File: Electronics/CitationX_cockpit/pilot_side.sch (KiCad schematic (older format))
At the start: 18 parts

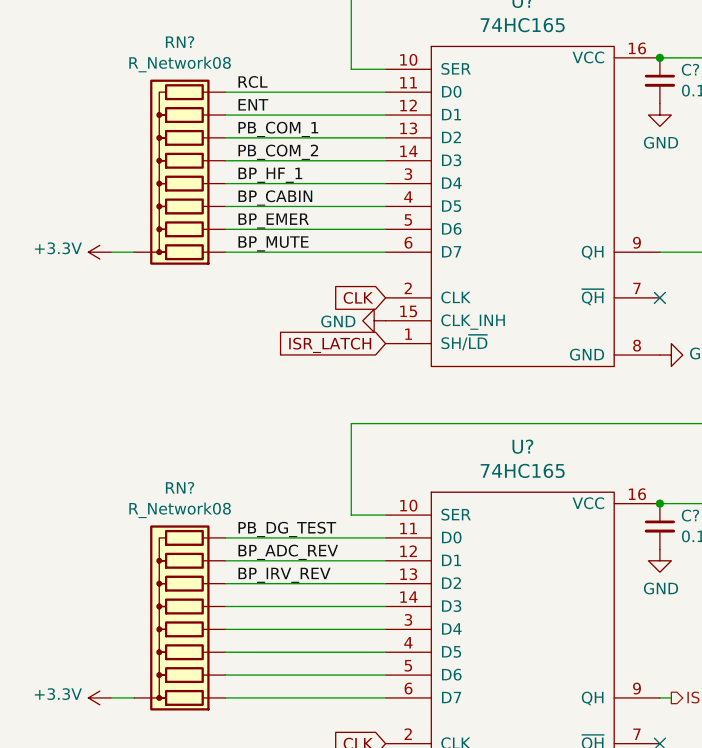
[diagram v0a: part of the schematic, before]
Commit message: Electronics - Working on copilot side and APU
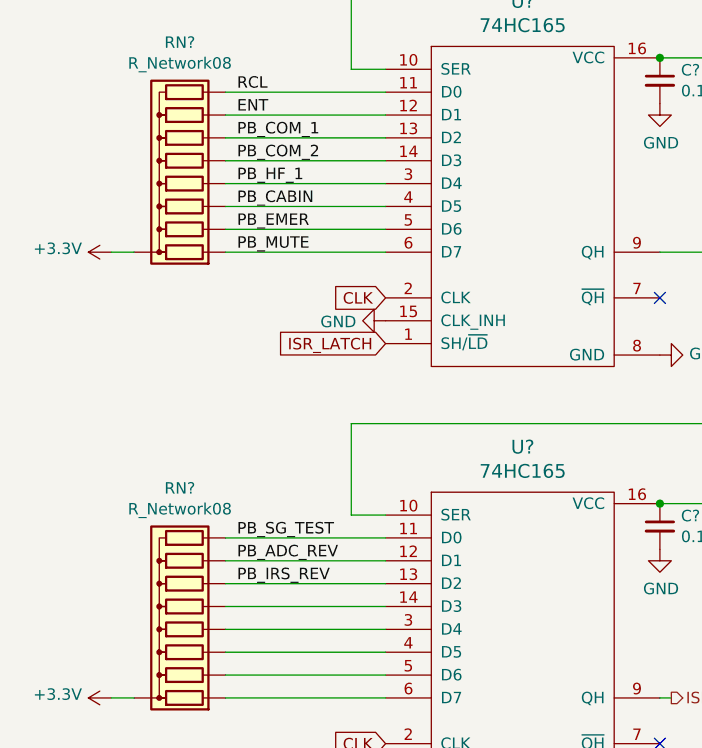
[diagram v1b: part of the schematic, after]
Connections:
- net BP_ADC_REV renamed PB_ADC_REV
- net BP_CABIN renamed PB_CABIN
- net BP_EMER renamed PB_EMER
- net BP_HF_1 renamed PB_HF_1
- net BP_IRV_REV renamed PB_IRS_REV
- net BP_MUTE renamed PB_MUTE
- net PB_DG_TEST renamed PB_SG_TEST
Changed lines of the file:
@@
 PB_COM_2
 Text Label 1600 5350 0    50   ~ 0
-BP_HF_1
+PB_HF_1
 Text Label 1600 5450 0    50   ~ 0
-BP_CABIN
+PB_CABIN
 Text Label 1600 5550 0    50   ~ 0
-BP_EMER
+PB_EMER
 Text Label 1600 5650 0    50   ~ 0
-BP_MUTE
+PB_MUTE
 Text Label 1600 6900 0    50   ~ 0
-PB_DG_TEST
+PB_SG_TEST
 Text Label 1600 7000 0    50   ~ 0
-BP_ADC_REV
+PB_ADC_REV
 Text Label 1600 7100 0    50   ~ 0
-BP_IRV_REV
+PB_IRS_REV
 $Comp
 L Device:C_Small C?

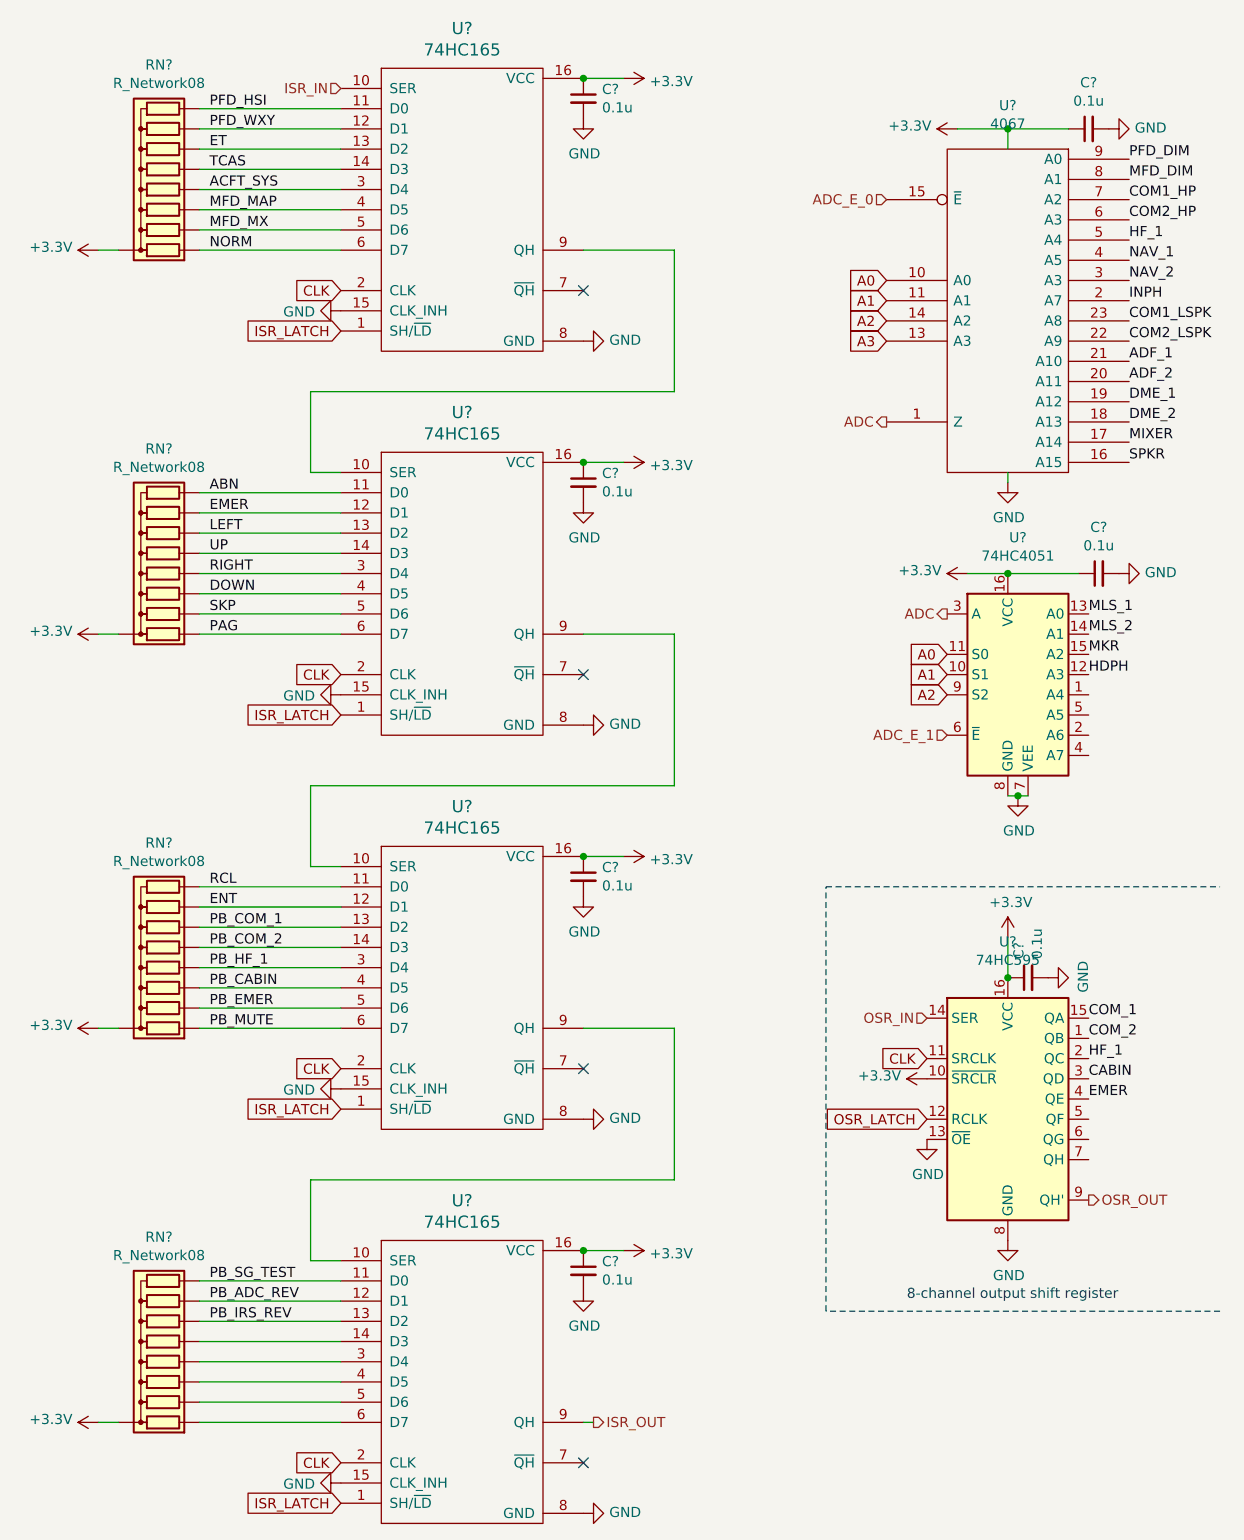
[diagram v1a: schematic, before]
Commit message: Electronics - Misc. works
Continued (and checked board). All connections are probably OK.
Fixed hierarchical pins in APUs (affects all schematics)
Numbered elements for testing schematics
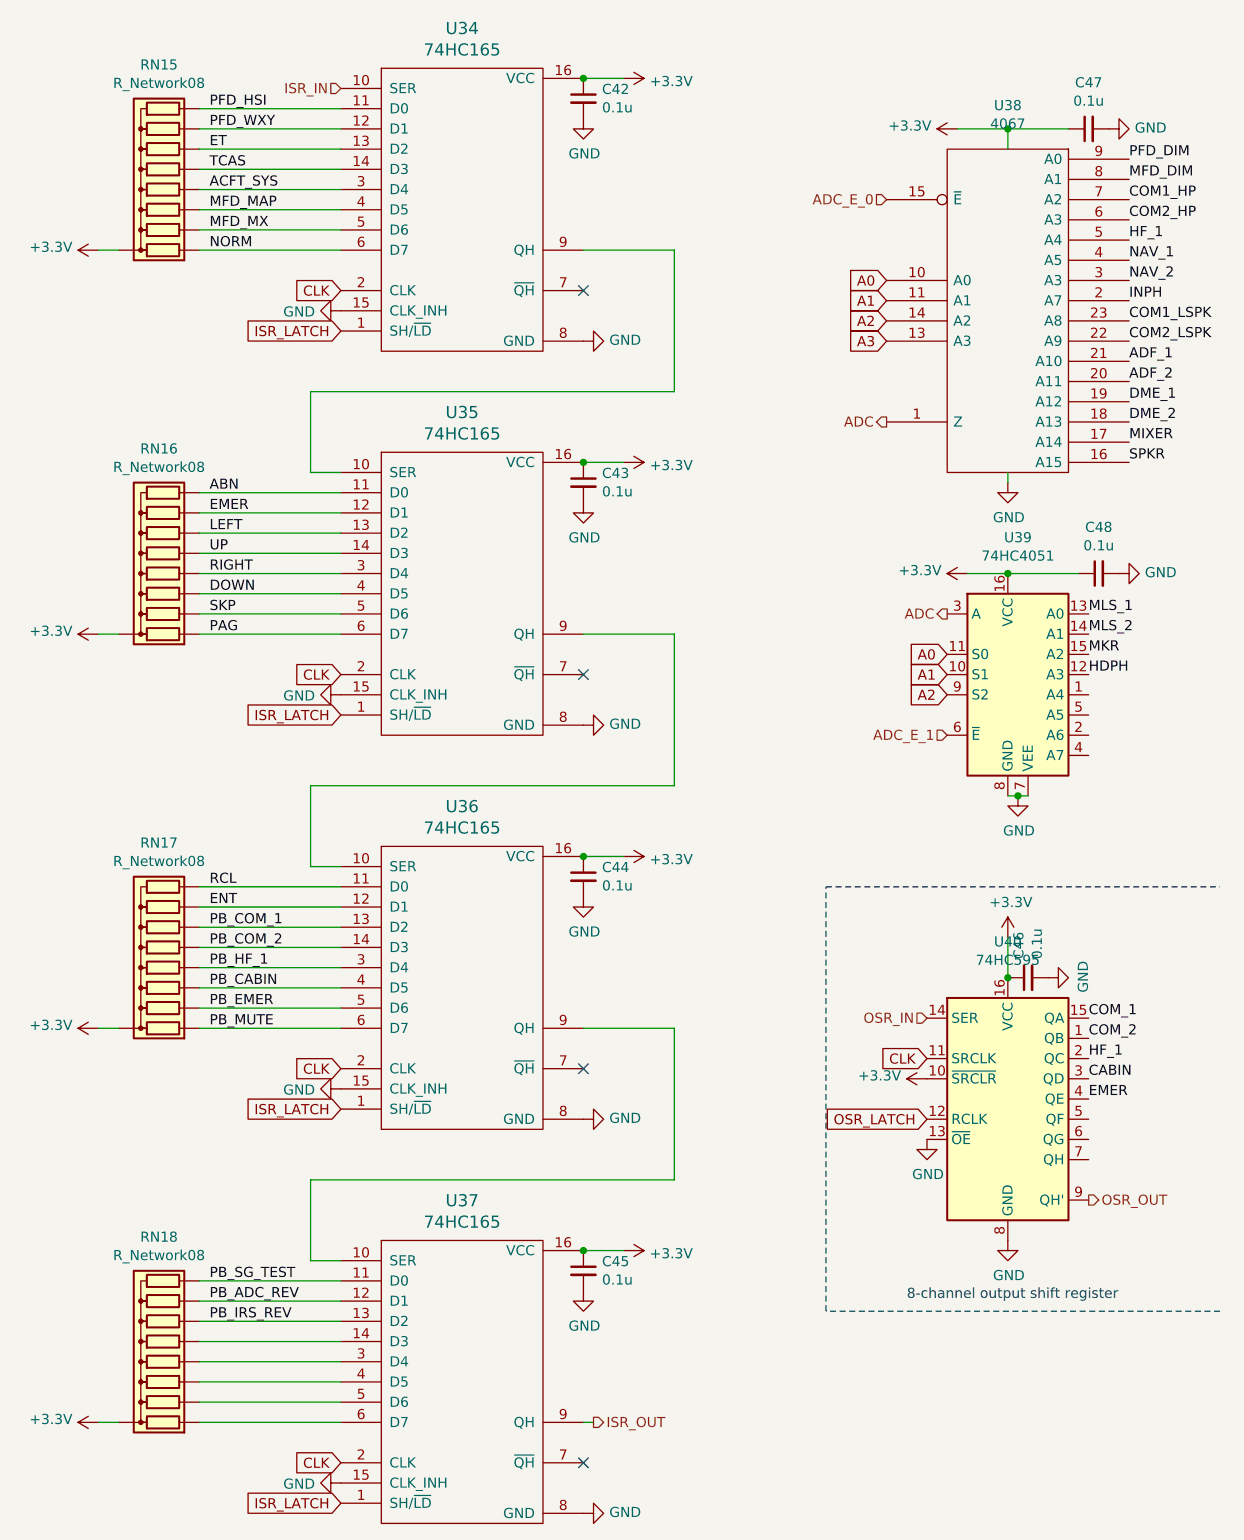
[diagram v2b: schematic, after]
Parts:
- gave numbers to parts that had none: 18
